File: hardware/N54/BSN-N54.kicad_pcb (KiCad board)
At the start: 4 copper layers, 34 x 34 mm, 44 parts, among them J1 Conn_Coaxial_Small, U1 nRF54L05-QFXX, U2 SHTC3, U3 HDC2010, X1 32MHz, X2 32.768kHz

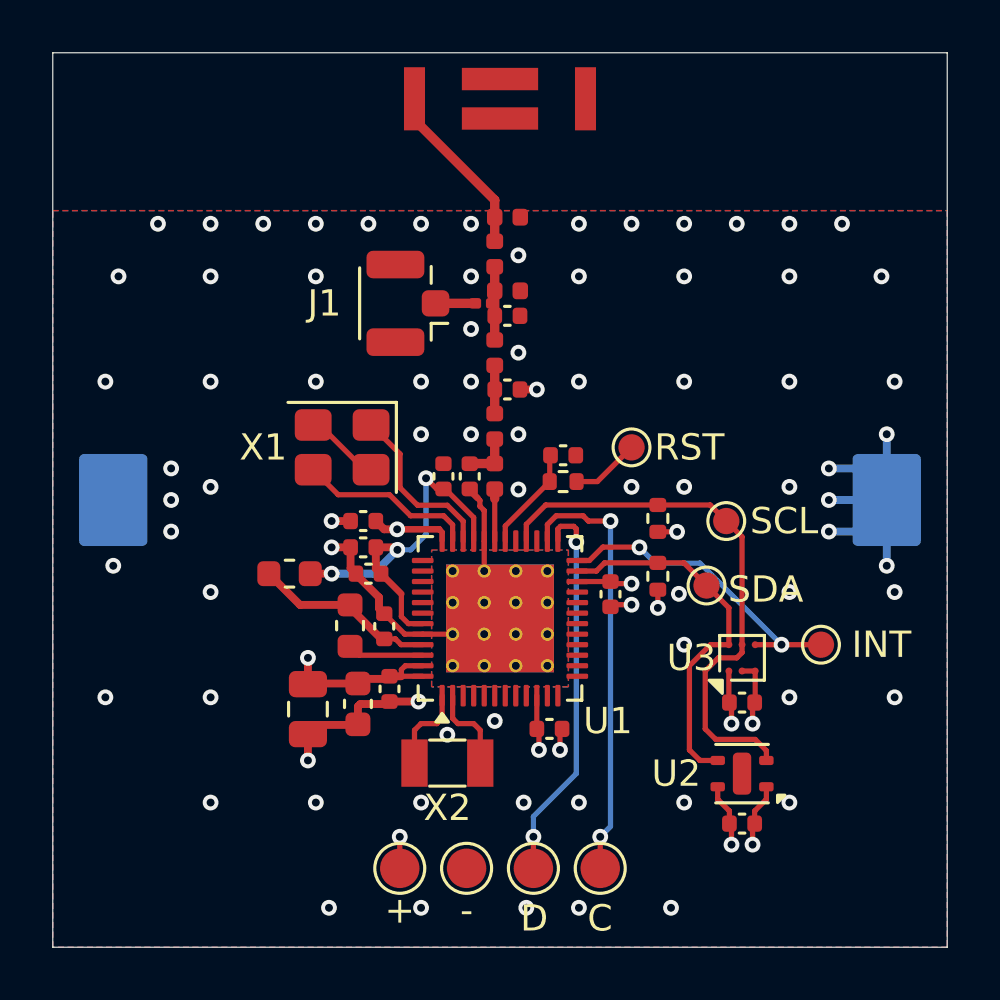
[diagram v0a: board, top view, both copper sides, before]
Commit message: Rounded tracks
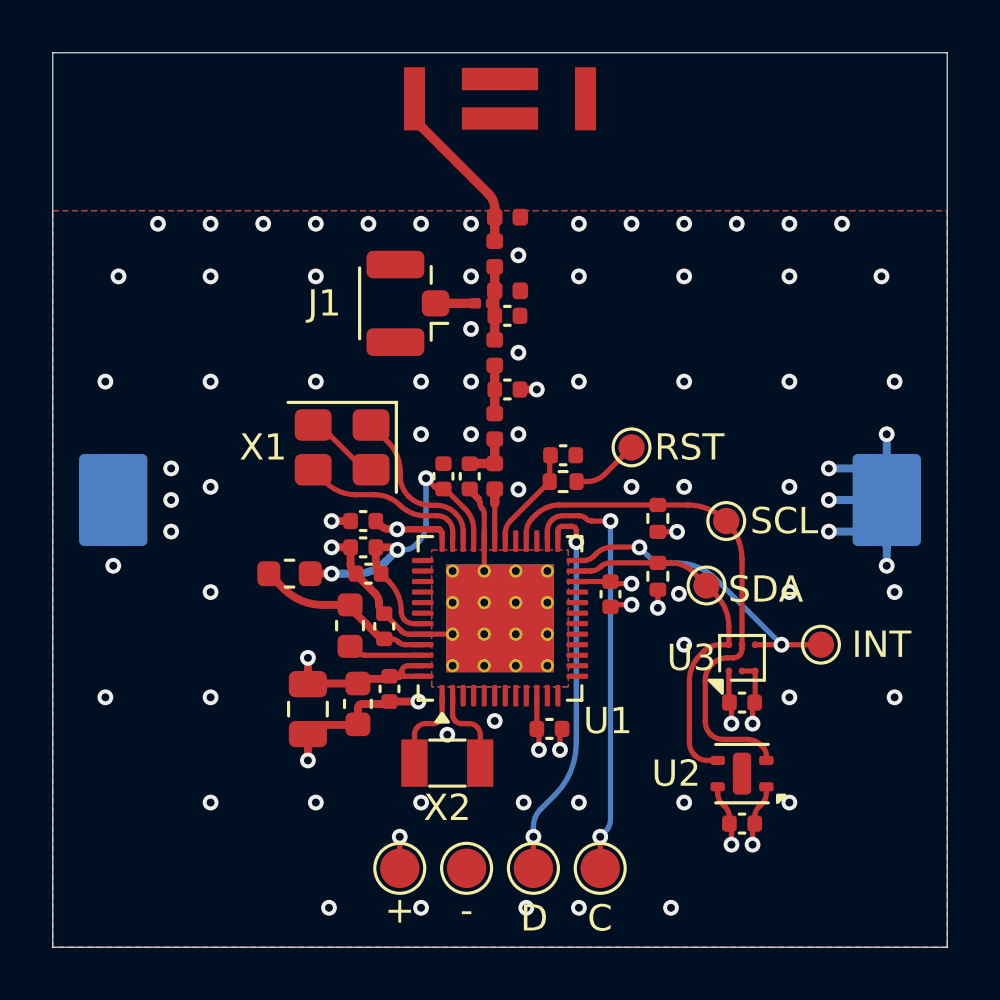
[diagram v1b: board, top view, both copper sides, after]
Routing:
- net VDD: track 32.5 -> 35.0 mm
- net /SCL: track 21.0 -> 20.4 mm

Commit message: Added some vias
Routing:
- net GND: vias 77 -> 80
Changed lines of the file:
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@@
 	)
 	(via
+		(at 156.6 107.5)
+		(size 0.6)
+		(drill 0.3)
+		(layers "F.Cu" "B.Cu")
+		(free yes)
+		(net "GND")
+	)
+	(via
 		(at 137.5 100)
 		(size 0.6)
@@
 	)
 	(via
+		(at 154.9 107.4)
+		(size 0.6)
+		(drill 0.3)
+		(layers "F.Cu" "B.Cu")
+		(free yes)
+		(net "GND")
+	)
+	(via
 		(at 153 91.5)
 		(size 0.6)
@@
 	)
 	(via
+		(at 153.6 107.4)
+		(size 0.6)
+		(drill 0.3)
+		(layers "F.Cu" "B.Cu")
+		(free yes)
+		(net "GND")
+	)
+	(via
 		(at 153 111.5)
 		(size 0.6)
@@
 		(layer "F.Cu")
 		(hatch none 0.1)
-		(priority 30033)
+		(priority 30032)
 		(attr
 			(teardrop
@@
 		(layer "F.Cu")
 		(hatch none 0.1)
-		(priority 30032)
+		(priority 30033)
 		(attr
 			(teardrop
@@
 		(polygon
 			(pts
-				(xy 149.9793 93.59) (xy 149.985342 93.500458) (xy 150.007638 93.396465) (xy 150.069343 93.223576)
-				(xy 149.8 92.999) (xy 149.530657 93.223576) (xy 149.579607 93.354477) (xy 149.607516 93.458679)
-				(xy 149.6207 93.59)
+				(xy 149.6207 92.41) (xy 149.614658 92.499542) (xy 149.592362 92.603535) (xy 149.530657 92.776424)
+				(xy 149.8 93.001) (xy 150.069343 92.776424) (xy 150.020393 92.645523) (xy 149.992484 92.541321)
+				(xy 149.9793 92.41)
 			)
 		)
@@
 		(polygon
 			(pts
-				(xy 149.6207 92.41) (xy 149.614658 92.499542) (xy 149.592362 92.603535) (xy 149.530657 92.776424)
-				(xy 149.8 93.001) (xy 150.069343 92.776424) (xy 150.020393 92.645523) (xy 149.992484 92.541321)
-				(xy 149.9793 92.41)
+				(xy 149.9793 93.59) (xy 149.985342 93.500458) (xy 150.007638 93.396465) (xy 150.069343 93.223576)
+				(xy 149.8 92.999) (xy 149.530657 93.223576) (xy 149.579607 93.354477) (xy 149.607516 93.458679)
+				(xy 149.6207 93.59)
 			)
 		)
@@
 	)
 	(zone
+		(layer "F.Cu")
+		(hatch edge 0.5)
+		(connect_pads
+			(clearance 0)
+		)
+		(min_thickness 0.15)
+		(keepout
+			(tracks allowed)
+			(vias allowed)
+			(pads allowed)
+			(copperpour not_allowed)
+			(footprints allowed)
+		)
+		(placement
+			(enabled no)
+			(sheetname "/")
+		)
+		(fill
+			(thermal_gap 0.5)
+			(thermal_bridge_width 0.3)
+			(island_removal_mode 0)
+		)
+		(polygon
+			(pts
+				(xy 143.65 104.025) (xy 144.3 104.025) (xy 144.3 105.525) (xy 143.65 105.525)
+			)
+		)
+	)
+	(zone
 		(net "GND")
 		(layer "F.Cu")
@@
 		(layer "F.Cu")
 		(hatch none 0.1)
-		(priority 30048)
+		(priority 30049)
 		(attr
 			(teardrop
@@
 		(layer "F.Cu")
 		(hatch none 0.1)
-		(priority 30049)
+		(priority 30048)
 		(attr
 			(teardrop
@@
 		(layer "F.Cu")
 		(hatch none 0.1)
-		(priority 30022)
+		(priority 30107)
 		(attr
 			(teardrop
@@
 		(polygon
 			(pts
-				(xy 157.269309 102.81073) (xy 157.317924 102.866187) (xy 157.348179 102.916049) (xy 157.368066 103.000369)
-				(xy 157.359854 103.095845) (xy 157.349403 103.192487) (xy 157.354278 103.315263) (xy 157.853731 103.253731)
-				(xy 157.915263 102.754278) (xy 157.771215 102.750843) (xy 157.695845 102.759854) (xy 157.625032 102.76779)
-				(xy 157.558587 102.762856) (xy 157.489491 102.733784) (xy 157.41073 102.669309)
+				(xy 157.923735 103.182313) (xy 157.823759 103.108655) (xy 157.701519 103.064899) (xy 157.636229 103.056733)
+				(xy 157.572897 103.058685) (xy 157.514878 103.070327) (xy 157.462707 103.091541) (xy 157.421979 103.119115)
+				(xy 157.389199 103.154532) (xy 157.367621 103.19331) (xy 157.354862 103.23845) (xy 157.354278 103.315263)
+				(xy 157.497154 102.897154) (xy 157.354278 103.315263) (xy 157.364232 103.354063) (xy 157.380904 103.376262)
+				(xy 157.421054 103.383929) (xy 157.492047 103.357483) (xy 157.521356 103.342659) (xy 157.587208 103.310722)
+				(xy 157.655156 103.288467) (xy 157.721444 103.288578) (xy 157.75279 103.300983) (xy 157.782313 103.323735)
 			)
 		)
@@
 		(layer "F.Cu")
 		(hatch none 0.1)
-		(priority 30107)
+		(priority 30022)
 		(attr
 			(teardrop
@@
 		(polygon
 			(pts
-				(xy 157.923735 103.182313) (xy 157.823759 103.108655) (xy 157.701519 103.064899) (xy 157.636229 103.056733)
-				(xy 157.572897 103.058685) (xy 157.514878 103.070327) (xy 157.462707 103.091541) (xy 157.421979 103.119115)
-				(xy 157.389199 103.154532) (xy 157.367621 103.19331) (xy 157.354862 103.23845) (xy 157.354278 103.315263)
-				(xy 157.497154 102.897154) (xy 157.354278 103.315263) (xy 157.364232 103.354063) (xy 157.380904 103.376262)
-				(xy 157.421054 103.383929) (xy 157.492047 103.357483) (xy 157.521356 103.342659) (xy 157.587208 103.310722)
-				(xy 157.655156 103.288467) (xy 157.721444 103.288578) (xy 157.75279 103.300983) (xy 157.782313 103.323735)
+				(xy 157.269309 102.81073) (xy 157.317924 102.866187) (xy 157.348179 102.916049) (xy 157.368066 103.000369)
+				(xy 157.359854 103.095845) (xy 157.349403 103.192487) (xy 157.354278 103.315263) (xy 157.853731 103.253731)
+				(xy 157.915263 102.754278) (xy 157.771215 102.750843) (xy 157.695845 102.759854) (xy 157.625032 102.76779)
+				(xy 157.558587 102.762856) (xy 157.489491 102.733784) (xy 157.41073 102.669309)
 			)
 		)
@@
 		(layer "F.Cu")
 		(hatch none 0.1)
-		(priority 30061)
+		(priority 30126)
 		(attr
 			(teardrop
@@
 		(polygon
 			(pts
-				(xy 160.102567 105.4) (xy 160.102567 105.6) (xy 160.585195 105.777164) (xy 160.703567 105.5) (xy 160.585195 105.222836)
+				(xy 160.702567 105.6) (xy 160.702567 105.4) (xy 160.402567 105.539158) (xy 160.401 105.5) (xy 160.402567 105.539158)
 			)
 		)
@@
 		(layer "F.Cu")
 		(hatch none 0.1)
-		(priority 30126)
+		(priority 30061)
 		(attr
 			(teardrop
@@
 		(polygon
 			(pts
-				(xy 160.702567 105.6) (xy 160.702567 105.4) (xy 160.402567 105.539158) (xy 160.401 105.5) (xy 160.402567 105.539158)
+				(xy 160.102567 105.4) (xy 160.102567 105.6) (xy 160.585195 105.777164) (xy 160.703567 105.5) (xy 160.585195 105.222836)
 			)
 		)

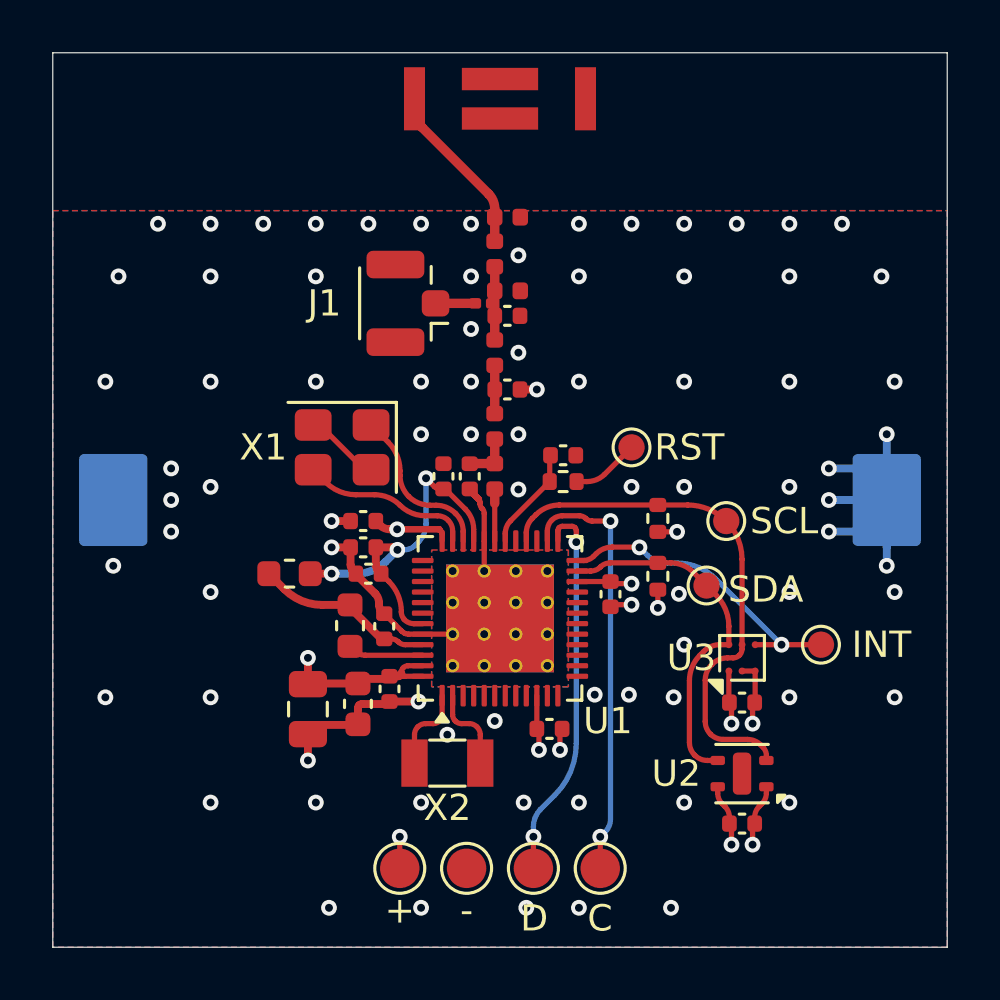
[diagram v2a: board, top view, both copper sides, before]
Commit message: Added UART test points
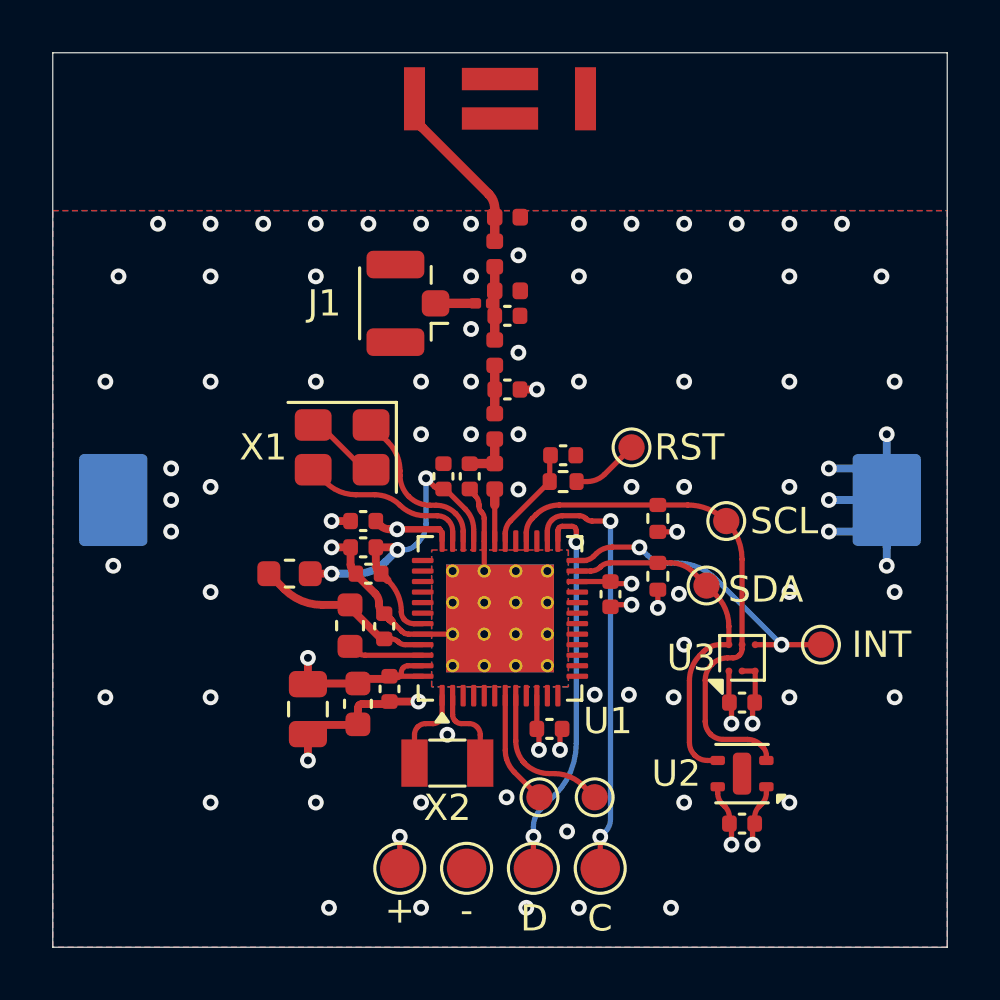
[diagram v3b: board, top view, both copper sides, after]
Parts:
- added TP10: TestPoint, TestPoint:TestPoint_Pad_D1.0mm, F.Cu at (153.6, 111.3)
- added TP9: TestPoint, TestPoint:TestPoint_Pad_D1.0mm, F.Cu at (151.5, 111.3)
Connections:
- U1 pad 7: unconnected-(U1-P1.06-Pad7) -> /TXD
- U1 pad 8: unconnected-(U1-P1.07-Pad8) -> /RXD
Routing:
- net /RXD: track 0.00 -> 5.72 mm
- net /TXD: track 0.00 -> 4.35 mm
- net GND: vias 80 -> 79

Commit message: Small routing fixes
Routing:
- net Net-(U1-SWDCLK): track 16.5 -> 17.2 mm
- net GND: vias 79 -> 78
